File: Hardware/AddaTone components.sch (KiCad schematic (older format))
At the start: 93 parts, among them J1 SWD_Header, J2 Conn_01x10_Female, J3 Conn_01x12_Female, J4 Conn_01x03_Male, J5 Conn_01x06_Male, J6 Conn_01x03_Male, J7 Conn_01x02_Male, J8 Eurorack_16_pin_power, U1 STM32F446RETx, U2 ICE40UP5K-SG48ITR, U3 MCP6004, U4 PCM5100APW, U5 TL072, U6 LD1117S12TR, U7 LM1117-3.3, Y1 ECS-12MHz

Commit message: Switched FPGA output to I2S DAC
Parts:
- U2: footprint Housings_DFN_QFN:QFN-48-1EP_7x7mm_Pitch0.5mm -> Custom_Footprints:ICE40_QFN-48-1EP_7x7mm_Pitch0.5mm
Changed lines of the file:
@@
 F 0 "U2" H 3650 8150 50  0000 L CNN
 F 1 "ICE40UP5K-SG48ITR" H 2250 7300 50  0000 L CNN
-F 2 "Housings_DFN_QFN:QFN-48-1EP_7x7mm_Pitch0.5mm" H 2650 5350 50  0001 C CNN
+F 2 "Custom_Footprints:ICE40_QFN-48-1EP_7x7mm_Pitch0.5mm" H 2650 5350 50  0001 C CNN
 F 3 "http://www.latticesemi.com/Products/FPGAandCPLD/iCE40Ultra" H 2100 8100 50  0001 C CNN
 	1    2650 7300

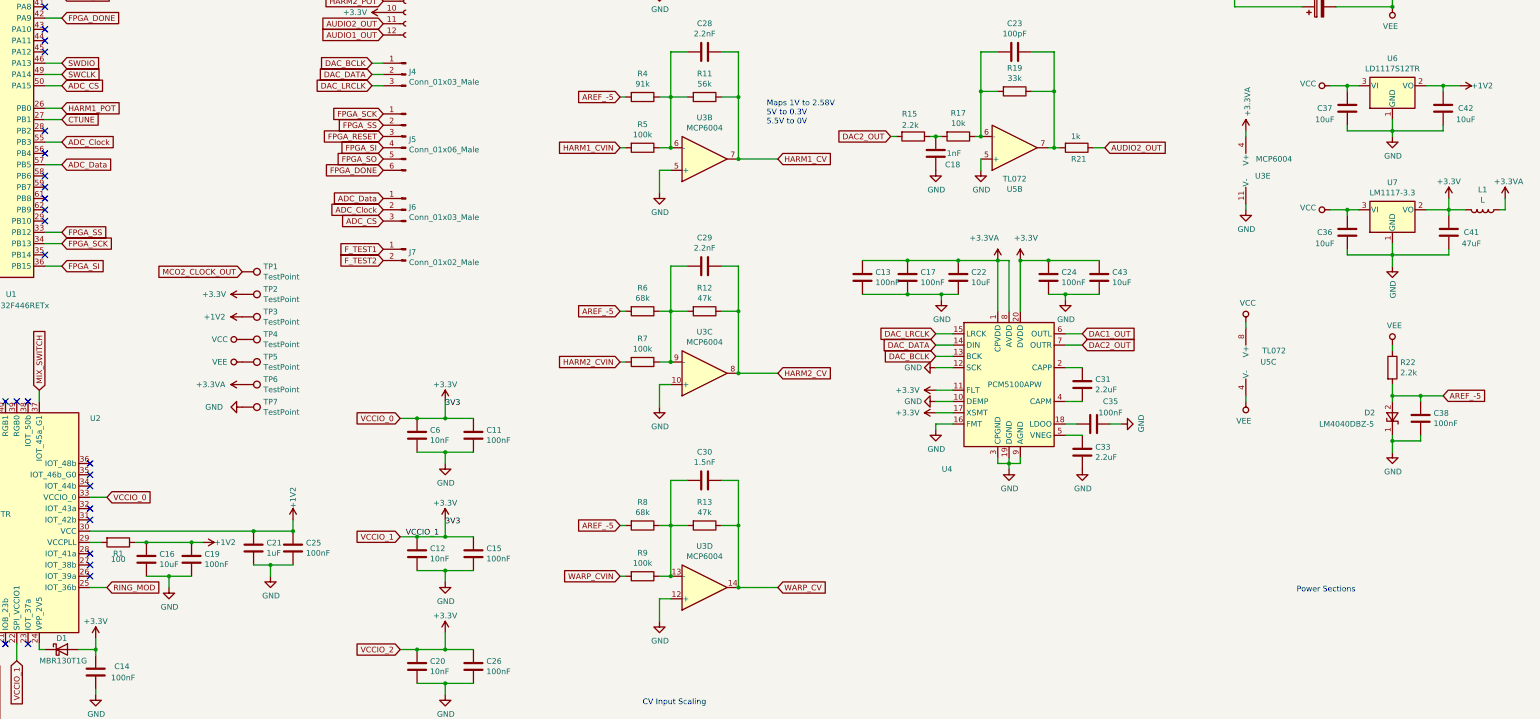
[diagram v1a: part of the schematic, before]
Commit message: Fixes to schematic (missing resistor on 1.2V LDO); Created new implementation to support production board; added FPGA tester project
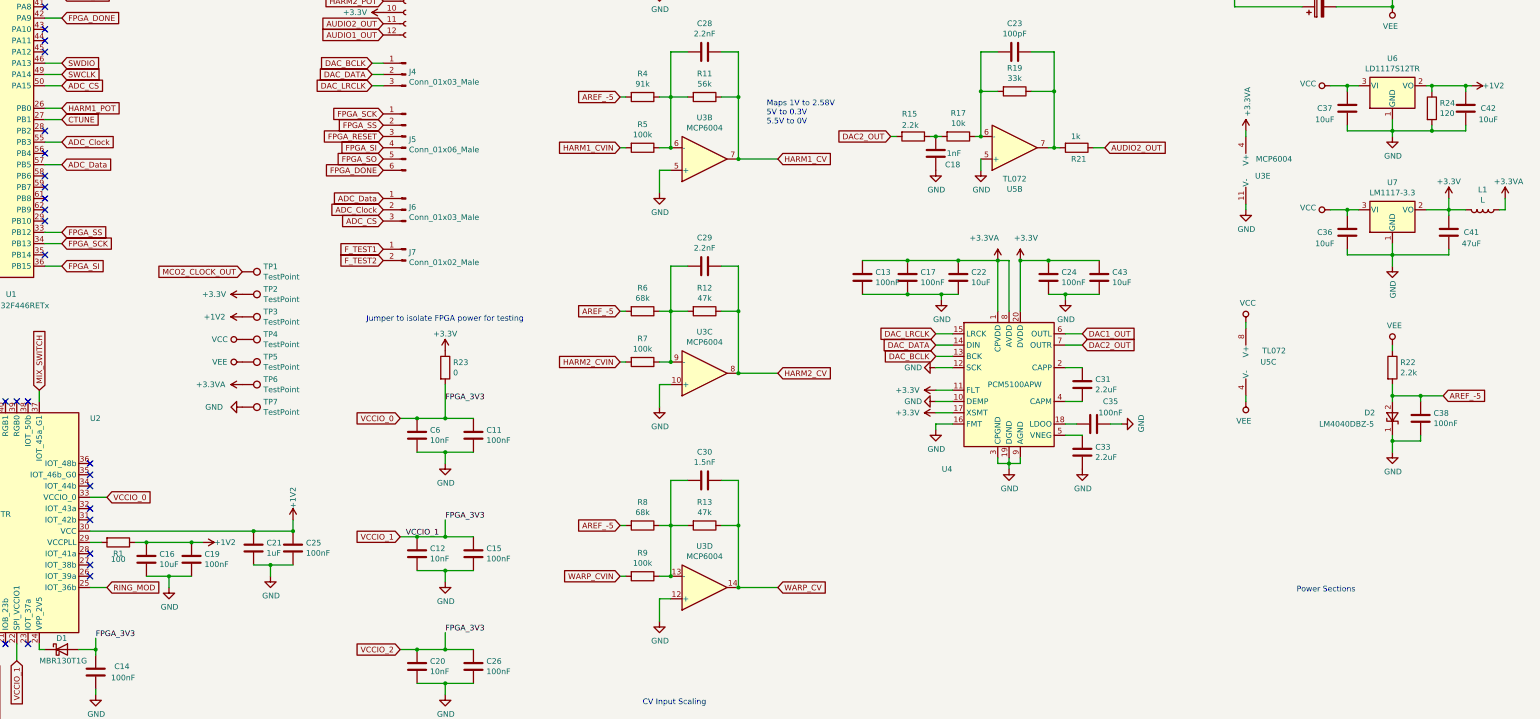
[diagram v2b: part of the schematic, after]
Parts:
- added R23: 0, Resistors_SMD:R_1206, symbol Device:R
- added R24: 120, Resistors_SMD:R_0805_HandSoldering, symbol Device:R
- U4: footprint Housings_SSOP:SSOP-20_4.4x6.5mm_Pitch0.65mm -> Custom_Footprints:SSOP-20_4.4x6.5mm_Pitch0.65mm_Round_Pads
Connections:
- net +1V2: now also R24.1
- net +3V3: now also R23.1; no longer C11.1, C12.1, C14.2, C15.1, C20.1, C26.1, C6.1, D1.2 (A), U2.1 (VCCIO_2), U2.22 (SPI_VCCIO1), U2.33 (VCCIO_0)
- net GND: now also R24.2
- new net VCCIO_0: C11.1, C12.1, C14.2, C15.1, C20.1, C26.1, C6.1, D1.2 (A), R23.2, U2.1 (VCCIO_2), U2.22 (SPI_VCCIO1), U2.33 (VCCIO_0)
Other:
- note added: "Jumper to isolate FPGA power for testing"
- moved on the sheet: C42
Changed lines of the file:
@@
 $EndComp
 Wire Wire Line
-	15500 3500 15650 3500
+	15500 3500 15550 3500
 $Comp
 L Device:C C37
@@
 L Device:C C42
 U 1 1 5E9BEF46
-P 15650 3700
-F 0 "C42" H 15850 3700 50  0000 C CNN
-F 1 "10uF" H 15850 3600 50  0000 C CNN
-F 2 "Capacitors_SMD:CP_Elec_3x5.3" H 15688 3550 50  0001 C CNN
-F 3 "~" H 15650 3700 50  0001 C CNN
-	1    15650 3700
+P 15850 3700
+F 0 "C42" H 16050 3700 50  0000 C CNN
+F 1 "10uF" H 16050 3600 50  0000 C CNN
+F 2 "Capacitors_SMD:CP_Elec_3x5.3" H 15888 3550 50  0001 C CNN
+F 3 "~" H 15850 3700 50  0001 C CNN
+	1    15850 3700
 	1    0    0    -1
 $EndComp
@@
 	15500 4600 15700 4600
 Wire Wire Line
-	15650 3500 15650 3550
+	15850 3500 15850 3550
 Wire Wire Line
 	15700 4950 15700 5000
@@
 	15200 3900 15200 3950
 Wire Wire Line
-	15650 3850 15650 3900
-Wire Wire Line
-	15650 3900 15200 3900
+	15850 3850 15850 3900
+Wire Wire Line
+	15850 3900 15550 3900
 $Comp
 L Device:C C7
@@
 Wire Wire Line
 	6550 7800 6800 7800
-$Comp
-L power:+3.3V #PWR016
-U 1 1 5F0D956C
-P 6800 7350
-F 0 "#PWR016" H 6800 7200 50  0001 C CNN
-F 1 "+3.3V" H 6800 7500 50  0000 C CNN
-F 2 "" H 6800 7350 50  0001 C CNN
-F 3 "" H 6800 7350 50  0001 C CNN
-	1    6800 7350
-	1    0    0    -1
-$EndComp
 Wire Wire Line
 	6800 7350 6800 7500
@@
 Wire Wire Line
 	6550 8800 6800 8800
-$Comp
-L power:+3.3V #PWR035
-U 1 1 5F15FF14
-P 6800 8350
-F 0 "#PWR035" H 6800 8200 50  0001 C CNN
-F 1 "+3.3V" H 6800 8500 50  0000 C CNN
-F 2 "" H 6800 8350 50  0001 C CNN
-F 3 "" H 6800 8350 50  0001 C CNN
-	1    6800 8350
-	1    0    0    -1
-$EndComp
 Wire Wire Line
 	6800 8350 6800 8500
@@
 L power:+3.3V #PWR08
 U 1 1 5F182DBD
-P 6800 6300
-F 0 "#PWR08" H 6800 6150 50  0001 C CNN
-F 1 "+3.3V" H 6800 6450 50  0000 C CNN
-F 2 "" H 6800 6300 50  0001 C CNN
-F 3 "" H 6800 6300 50  0001 C CNN
-	1    6800 6300
-	1    0    0    -1
-$EndComp
-Wire Wire Line
-	6800 6300 6800 6450
+P 6800 5850
+F 0 "#PWR08" H 6800 5700 50  0001 C CNN
+F 1 "+3.3V" H 6800 6000 50  0000 C CNN
+F 2 "" H 6800 5850 50  0001 C CNN
+F 3 "" H 6800 5850 50  0001 C CNN
+	1    6800 5850
+	1    0    0    -1
+$EndComp
 Text GLabel 6400 6450 0    50   Input ~ 0
 VCCIO_0
@@
 	1    4650 7550
 	0    1    1    0
-$EndComp
-$Comp
-L power:+3.3V #PWR018
-U 1 1 5EFA8BDD
-P 3700 8400
-F 0 "#PWR018" H 3700 8250 50  0001 C CNN
-F 1 "+3.3V" H 3700 8550 50  0000 C CNN
-F 2 "" H 3700 8400 50  0001 C CNN
-F 3 "" H 3700 8400 50  0001 C CNN
-	1    3700 8400
-	1    0    0    -1
 $EndComp
 Wire Wire Line
@@
 L power:+1V2 #PWR067
 U 1 1 5F159EF3
-P 15800 3500
-F 0 "#PWR067" H 15800 3350 50  0001 C CNN
-F 1 "+1V2" V 15800 3600 50  0000 L CNN
-F 2 "" H 15800 3500 50  0001 C CNN
-F 3 "" H 15800 3500 50  0001 C CNN
-	1    15800 3500
-	0    1    1    0
-$EndComp
-Wire Wire Line
-	15650 3500 15800 3500
+P 15900 3500
+F 0 "#PWR067" H 15900 3350 50  0001 C CNN
+F 1 "+1V2" V 15900 3600 50  0000 L CNN
+F 2 "" H 15900 3500 50  0001 C CNN
+F 3 "" H 15900 3500 50  0001 C CNN
+	1    15900 3500
+	0    1    1    0
+$EndComp
 $Comp
 L Device:C C36
@@
 Wire Wire Line
 	14800 4950 14800 5000
-Connection ~ 15650 3500
+Connection ~ 15850 3500
 Wire Wire Line
 	14800 5000 15200 5000
@@
 F 0 "U4" H 11250 5300 50  0000 C CNN
 F 1 "PCM5100APW" H 11850 6050 50  0000 C CNN
-F 2 "Housings_SSOP:SSOP-20_4.4x6.5mm_Pitch0.65mm" H 11750 6850 50  0001 C CNN
+F 2 "Custom_Footprints:SSOP-20_4.4x6.5mm_Pitch0.65mm_Round_Pads" H 11750 6850 50  0001 C CNN
 F 3 "http://www.ti.com/lit/ds/symlink/pcm5100.pdf" H 11750 6850 50  0001 C CNN
 	1    11800 6100
@@
 Text GLabel 6150 3500 0    50   Input ~ 0
 DAC_LRCLK
-Text Label 6800 6350 0    50   ~ 0
-3V3
 Text Label 6450 7500 0    50   ~ 0
 VCCIO_1
-Text Label 6800 7400 0    50   ~ 0
-3V3
 Connection ~ 15200 5000
 Wire Wire Line
@@
 	0    1    1    0
 $EndComp
+$Comp
+L Device:R R23
+U 1 1 5EC432F3
+P 6800 6000
+F 0 "R23" H 6870 6046 50  0000 L CNN
+F 1 "0" H 6870 5955 50  0000 L CNN
+F 2 "Resistors_SMD:R_1206" V 6730 6000 50  0001 C CNN
+F 3 "~" H 6800 6000 50  0001 C CNN
+	1    6800 6000
+	1    0    0    -1
+$EndComp
+Text Label 6800 6300 0    50   ~ 0
+FPGA_3V3
+Wire Wire Line
+	6800 6150 6800 6450
+Text Label 6800 7350 0    50   ~ 0
+FPGA_3V3
+Text Label 6800 8350 0    50   ~ 0
+FPGA_3V3
+Text Notes 6100 5600 0    50   ~ 0
+Jumper to isolate FPGA power for testing
+Text Label 3700 8400 0    50   ~ 0
+FPGA_3V3
+$Comp
+L Device:R R24
+U 1 1 5ED48518
+P 15550 3700
+F 0 "R24" H 15620 3746 50  0000 L CNN
+F 1 "120" H 15620 3655 50  0000 L CNN
+F 2 "Resistors_SMD:R_0805_HandSoldering" V 15480 3700 50  0001 C CNN
+F 3 "~" H 15550 3700 50  0001 C CNN
+	1    15550 3700
+	1    0    0    -1
+$EndComp
+Wire Wire Line
+	15850 3500 15900 3500
+Wire Wire Line
+	15550 3550 15550 3500
+Connection ~ 15550 3500
+Wire Wire Line
+	15550 3500 15850 3500
+Wire Wire Line
+	15550 3850 15550 3900
+Connection ~ 15550 3900
+Wire Wire Line
+	15550 3900 15200 3900
 $EndSCHEMATC
